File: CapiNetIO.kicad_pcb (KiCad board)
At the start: 2 copper layers, 140 x 100 mm, 91 parts, among them J1 USB_B_Micro, J5 Conn_02x05_Counter_Clockwise, Q1 MMBT2222A, Q2 MMBT2222A, Q3 MMBT2222A, Q4 MMBT2222A, SW1 SW_SPDT, U1 STM32F446RETx, U3 AMS1117-3.3, Y1 16MHz

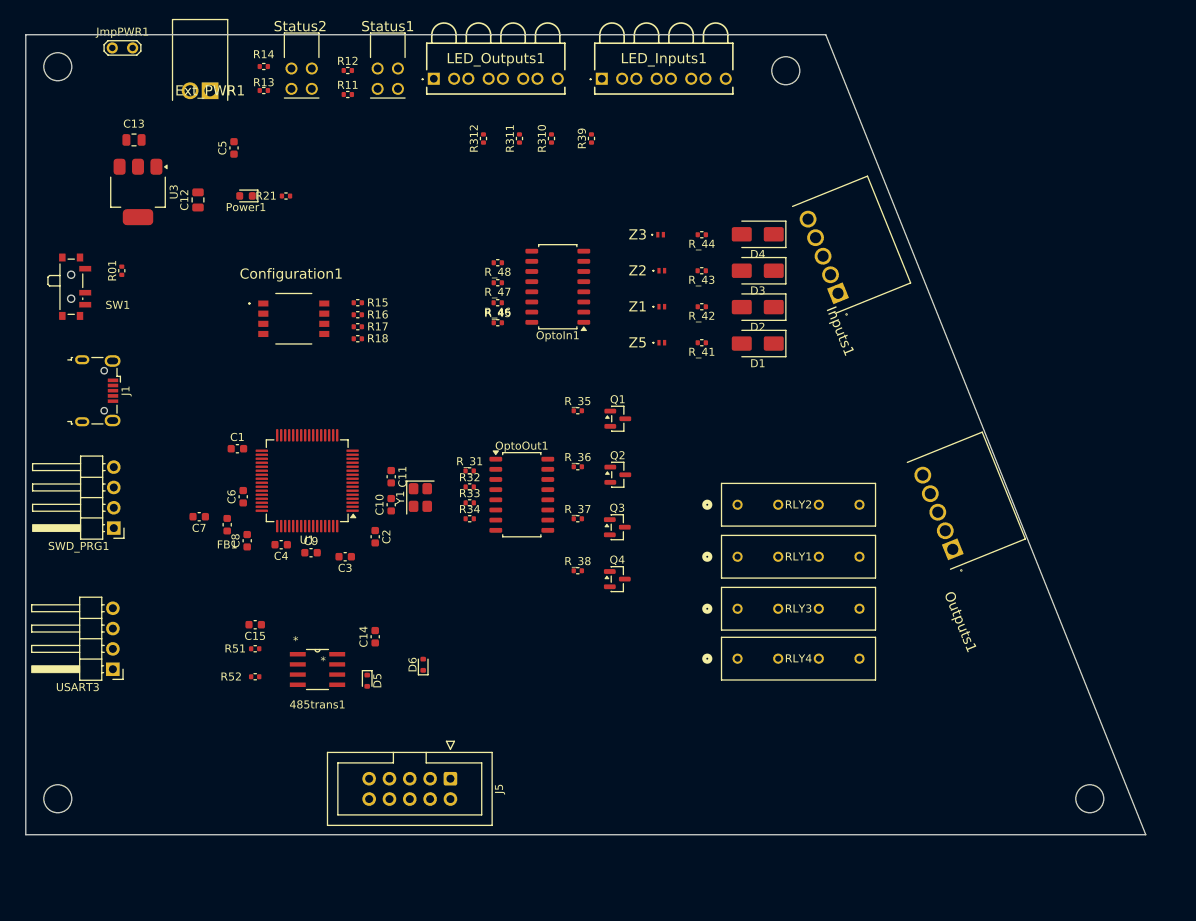
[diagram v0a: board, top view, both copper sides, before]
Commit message: working on the pcb side, tidying up io
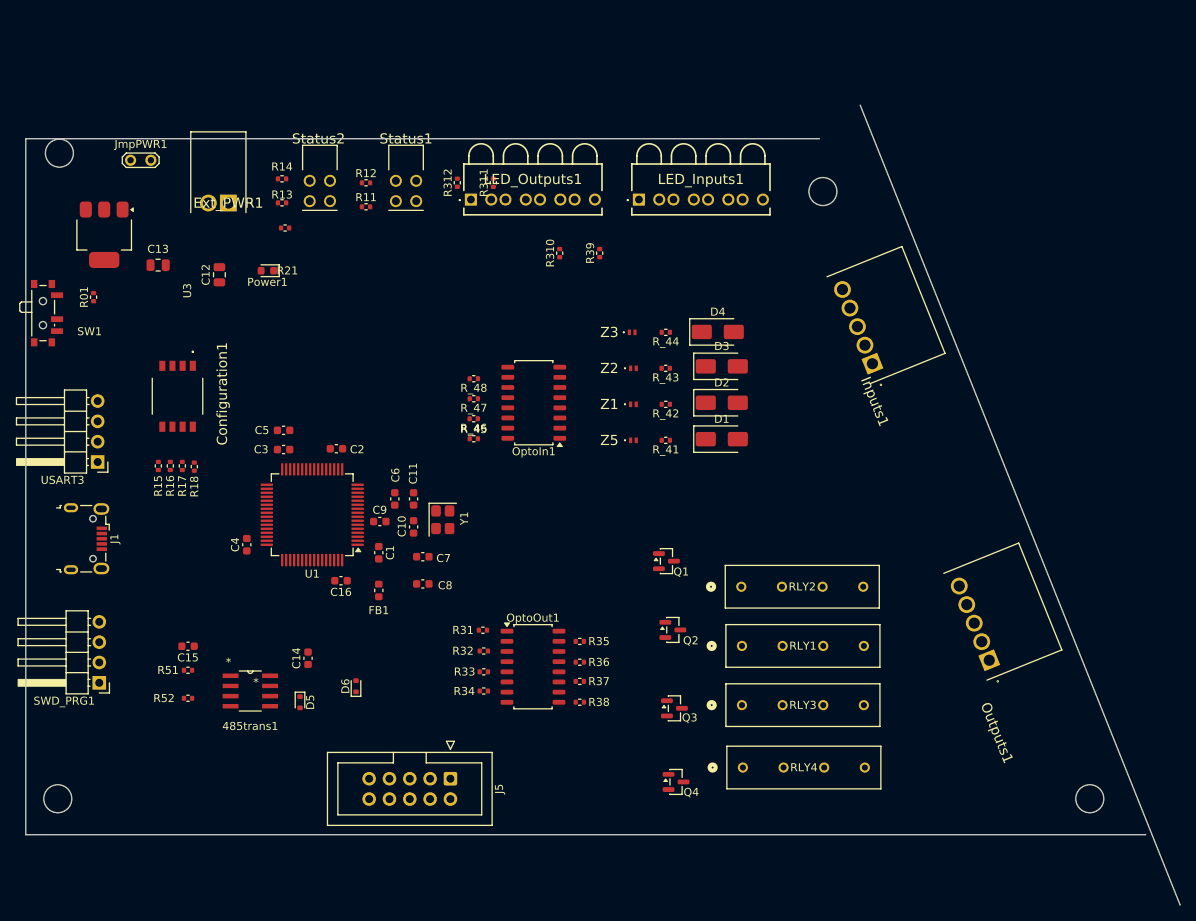
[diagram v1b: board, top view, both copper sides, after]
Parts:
- removed R_31: 390, Resistor_SMD:R_0402_1005Metric
- removed R_35, R_36, R_38: 4k7, Resistor_SMD:R_0402_1005Metric
- removed R_37: 4K7, Resistor_SMD:R_0402_1005Metric
- added C16: 100n, Capacitor_SMD:C_0603_1608Metric, F.Cu at (79.4, 98.2)
- added R31: 390, Resistor_SMD:R_0402_1005Metric, F.Cu at (97.1, 104.4)
- added R35: 4k7, Resistor_SMD:R_0402_1005Metric, F.Cu at (109.2, 105.8)
- added R36: 4k7, Resistor_SMD:R_0402_1005Metric, F.Cu at (109.2, 108.4)
- added R37: 4K7, Resistor_SMD:R_0402_1005Metric, F.Cu at (109.2, 110.8)
- added R38: 4k7, Resistor_SMD:R_0402_1005Metric, F.Cu at (109.2, 113.4)
- moved C5 35.8 mm to (72.2, 79.5), turned to 0 degrees
- moved R15 32.2 mm to (56.6, 83.9), turned to -90 degrees
- moved R16 30.1 mm to (58.1, 83.9), turned to -90 degrees
- moved C7 28.4 mm to (89.6, 95.2), turned to 0 degrees
- moved R17 28.0 mm to (59.6, 83.9), turned to -90 degrees
- moved Q4 26.4 mm to (121.3, 123.4)
- moved USART3 26.0 mm to (49.0, 83.4)
- moved R18 25.9 mm to (61.1, 84.0), turned to -90 degrees
- moved Q3 23.7 mm to (121.1, 114.2)
- moved C8 22.6 mm to (89.6, 98.7), turned to 0 degrees
- moved C1 21.9 mm to (84.1, 94.8), turned to -90 degrees
- moved R34 21.6 mm to (97.2, 112.0)
- moved OptoOut1 21.5 mm to (103.4, 109.0)
- moved R33 21.2 mm to (97.2, 109.6)
- moved FB1 20.7 mm to (84.1, 99.5)
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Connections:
- Configuration1 pad 5: /Config3 -> /Config0
- Configuration1 pad 6: /Config2 -> /Config1
- Configuration1 pad 7: /Config1 -> /Config2
- Configuration1 pad 8: /Config0 -> /Config3
- Inputs1 pad 2: Net-(D1-K) -> Net-(D1-A)
- Inputs1 pad 3: Net-(D2-K) -> Net-(D2-A)
- Inputs1 pad 4: Net-(D3-K) -> Net-(D3-A)
- Inputs1 pad 5: Net-(D4-K) -> Net-(D4-A)
- R_41 pad 1: Net-(D1-A) -> Net-(D1-K)
- R_42 pad 1: Net-(D2-A) -> Net-(D2-K)
- R_43 pad 1: Net-(D3-A) -> Net-(D3-K)
- R_44 pad 1: Net-(D4-A) -> Net-(D4-K)
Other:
- board size 140 x 100 mm -> 144.3 x 100 mm
